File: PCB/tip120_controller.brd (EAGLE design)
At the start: 52.4 x 37.5 mm, 14 parts, among them J1 AUDIO_JACK_3.5MM_PTH, Q1 TIP120

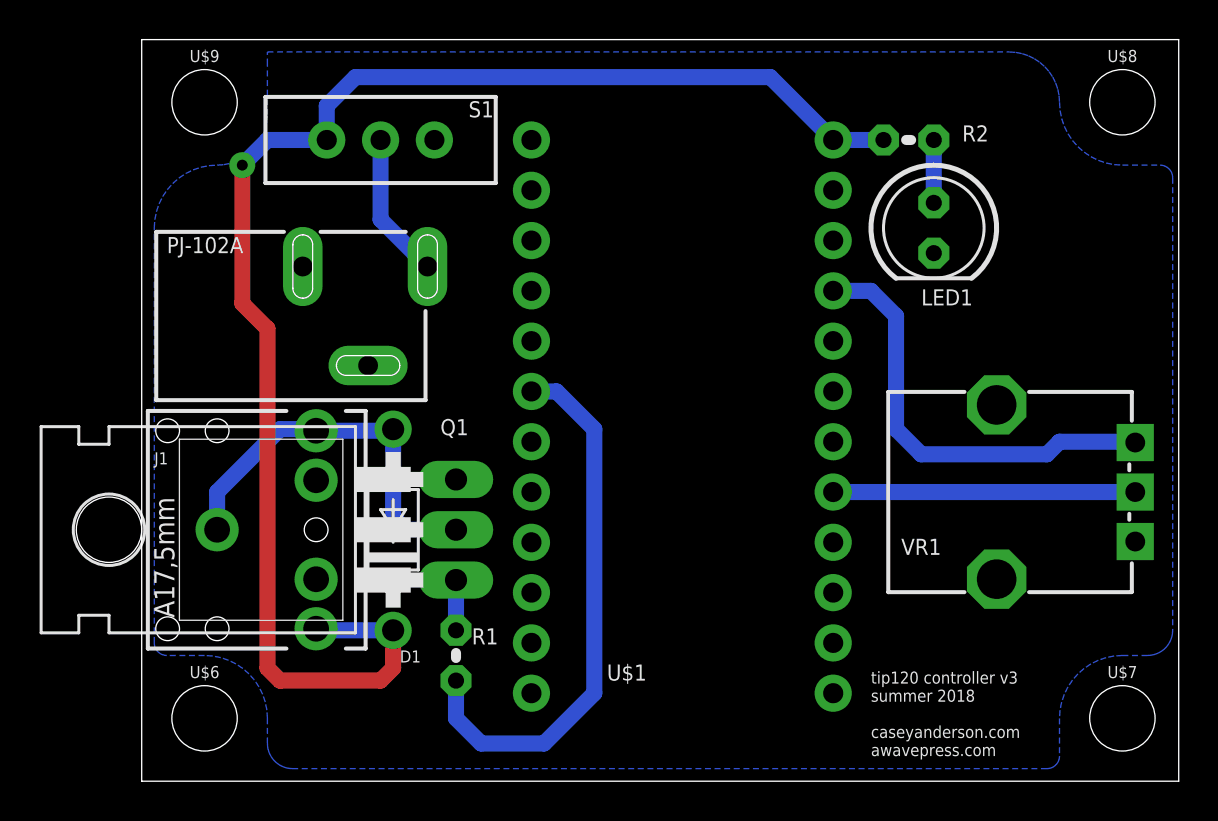
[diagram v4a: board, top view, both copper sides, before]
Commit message: replaced transistor symbol/footprint, futzing with silkscreen
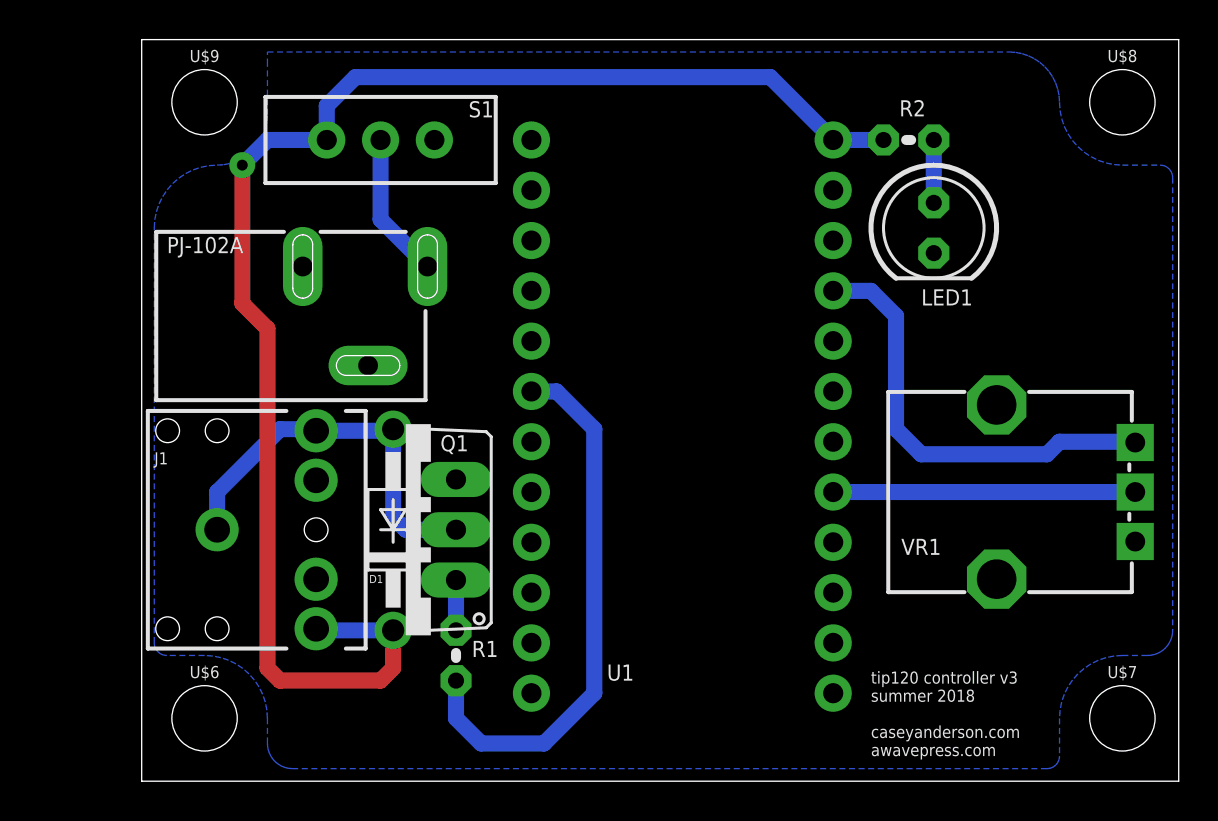
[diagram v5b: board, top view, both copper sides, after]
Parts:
- Q1: device transistor-power:TO220AH -> transistor-power:TO220AV
- moved Q1 3.81 mm to (12.7, 59.1)
- renumbered U$1 to U1
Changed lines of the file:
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@@
 </autorouter>
 <elements>
-<element name="U$1" library="SparkFun-Boards" package="ARDUINO_MINI" value="ARDUINO_MINI" x="26.67" y="66.04" smashed="yes">
+<element name="U1" library="SparkFun-Boards" package="ARDUINO_MINI" value="ARDUINO_MINI" x="26.67" y="66.04" smashed="yes">
 <attribute name="NAME" x="22.86" y="51.435" size="0.8128" layer="25" font="vector" ratio="15"/>
 <attribute name="VALUE" x="22.86" y="50.165" size="0.8128" layer="27" font="vector" ratio="15"/>
@@
 <attribute name="PROD_ID" value="SWCH-08261" x="11.43" y="78.74" size="1.778" layer="27" rot="R270" display="off"/>
 <attribute name="SF_SKU" value="COM-00102" x="11.43" y="78.74" size="1.778" layer="27" rot="R270" display="off"/>
-<attribute name="VALUE" x="15.24" y="77.597" size="0.8128" layer="27" font="vector" ratio="15" align="top-center"/>
 </element>
 <element name="R2" library="resistor" library_urn="urn:adsk.eagle:library:348" package="0204V" package3d_urn="urn:adsk.eagle:package:25948/1" value="220" x="38.1" y="78.74" smashed="yes" rot="R180">
-<attribute name="NAME" x="42.1386" y="79.4766" size="0.8128" layer="25" font="vector" ratio="15" rot="R180"/>
-<attribute name="VALUE" x="42.7736" y="78.5114" size="0.8128" layer="27" font="vector" ratio="15" rot="R180"/>
+<attribute name="NAME" x="38.9636" y="80.7466" size="0.8128" layer="25" font="vector" ratio="15" rot="R180"/>
 </element>
 <element name="LED1" library="led" library_urn="urn:adsk.eagle:library:259" package="LED5MM" package3d_urn="urn:adsk.eagle:package:15799/2" value="" x="39.37" y="74.295" smashed="yes" rot="R270">
 <attribute name="NAME" x="38.735" y="70.3834" size="0.8128" layer="25" font="vector" ratio="15"/>
 </element>
-<element name="Q1" library="transistor-power" library_urn="urn:adsk.eagle:library:400" package="TO220AH" package3d_urn="urn:adsk.eagle:package:29488/1" value="TIP120" x="8.89" y="59.055" smashed="yes" rot="R90">
-<attribute name="NAME" x="15.875" y="64.643" size="0.8128" layer="25" font="vector" ratio="15" rot="R180"/>
-<attribute name="VALUE" x="17.272" y="63.5" size="0.8128" layer="27" font="vector" ratio="15" rot="R180"/>
-</element>
 <element name="R1" library="resistor" library_urn="urn:adsk.eagle:library:348" package="0204V" package3d_urn="urn:adsk.eagle:package:25948/1" value="2.2k" x="15.24" y="52.705" smashed="yes" rot="R270">
-<attribute name="NAME" x="17.3736" y="54.0766" size="0.8128" layer="25" font="vector" ratio="15" rot="R180"/>
-<attribute name="VALUE" x="17.3736" y="53.1114" size="0.8128" layer="27" font="vector" ratio="15" rot="R180"/>
+<attribute name="NAME" x="17.3736" y="53.4416" size="0.8128" layer="25" font="vector" ratio="15" rot="R180"/>
 </element>
 <element name="J1" library="SparkFun-Connectors" package="AUDIO-JACK" value="AUDIO_JACK_3.5MM_PTH" x="3.175" y="59.055" smashed="yes">
@@
 </element>
 <element name="D1" library="diode" library_urn="urn:adsk.eagle:library:210" package="DO41-10" package3d_urn="urn:adsk.eagle:package:43336/1" value="1N4004" x="12.065" y="59.055" smashed="yes" rot="R90">
-<attribute name="NAME" x="13.462" y="52.959" size="0.6096" layer="25" font="vector" ratio="15" rot="R180"/>
+<attribute name="NAME" x="11.557" y="56.769" size="0.4064" layer="25" font="vector" ratio="15" rot="R180"/>
 </element>
 <element name="U$6" library="SparkFun-Hardware" package="STAND-OFF" value="" x="2.54" y="49.53"/>
@@
 <element name="U$8" library="SparkFun-Hardware" package="STAND-OFF" value="" x="48.895" y="80.645"/>
 <element name="U$9" library="SparkFun-Hardware" package="STAND-OFF" value="" x="2.54" y="80.645"/>
+<element name="Q1" library="transistor-power" library_urn="urn:adsk.eagle:library:400" package="TO220AV" package3d_urn="urn:adsk.eagle:package:29487/2" value="TIP120" x="12.7" y="59.055" smashed="yes" rot="R90">
+<attribute name="NAME" x="15.875" y="63.8302" size="0.8128" layer="25" font="vector" ratio="15" rot="R180"/>
+</element>
 </elements>
 <signals>
 <signal name="AGND">
-<contactref element="U$1" pad="23"/>
+<contactref element="U1" pad="23"/>
 <contactref element="LED1" pad="K"/>
 <contactref element="PJ-102A" pad="3"/>
 <contactref element="PJ-102A" pad="2"/>
-<contactref element="Q1" pad="E"/>
-<contactref element="U$1" pad="4"/>
+<contactref element="U1" pad="4"/>
 <contactref element="VR1" pad="P$1"/>
 <polygon width="0.254" layer="16" isolate="0.8128">
@@
 <vertex x="5.715" y="82.55"/>
 </polygon>
+<contactref element="Q1" pad="E"/>
 </signal>
 <signal name="N$3">
@@
 <wire x1="11.43" y1="74.72" x2="11.43" y2="78.74" width="0.8128" layer="16"/>
 </signal>
-<signal name="N$2">
-<contactref element="Q1" pad="B"/>
-<contactref element="R1" pad="1"/>
-<wire x1="15.24" y1="53.975" x2="15.24" y2="56.515" width="0.8128" layer="16"/>
-</signal>
 <signal name="N$8">
 <contactref element="S1" pad="3"/>
 <contactref element="R2" pad="2"/>
-<contactref element="U$1" pad="24"/>
+<contactref element="U1" pad="24"/>
 <wire x1="34.29" y1="78.74" x2="36.83" y2="78.74" width="0.8128" layer="16"/>
 <contactref element="J1" pad="TIP"/>
@@
 <signal name="N$1">
 <contactref element="R1" pad="2"/>
-<contactref element="U$1" pad="6"/>
+<contactref element="U1" pad="6"/>
 <wire x1="22.225" y1="50.8" x2="22.225" y2="64.135" width="0.8128" layer="16"/>
 <wire x1="22.225" y1="64.135" x2="20.32" y2="66.04" width="0.8128" layer="16"/>
@@
 <contactref element="J1" pad="RING"/>
 <contactref element="J1" pad="SLEEVE"/>
-<contactref element="Q1" pad="C"/>
 <contactref element="D1" pad="A"/>
 <wire x1="3.175" y1="59.055" x2="3.175" y2="60.96" width="0.8128" layer="16"/>
@@
 <wire x1="8.175" y1="64.055" x2="11.985" y2="64.055" width="0.8128" layer="16"/>
 <wire x1="11.985" y1="64.055" x2="12.065" y2="64.135" width="0.8128" layer="16"/>
-<wire x1="15.24" y1="59.055" x2="12.7" y2="59.055" width="0.8128" layer="16"/>
-<wire x1="12.7" y1="59.055" x2="12.065" y2="59.69" width="0.8128" layer="16"/>
+<wire x1="12.065" y1="59.69" x2="12.7" y2="59.055" width="0.8128" layer="16"/>
 <wire x1="12.065" y1="59.69" x2="12.065" y2="64.135" width="0.8128" layer="16"/>
+<contactref element="Q1" pad="C"/>
+<wire x1="12.7" y1="59.055" x2="15.24" y2="59.055" width="0.8128" layer="16"/>
 </signal>
 <signal name="N$5">
-<contactref element="U$1" pad="21"/>
+<contactref element="U1" pad="21"/>
 <contactref element="VR1" pad="P$3"/>
 <wire x1="34.29" y1="71.12" x2="36.195" y2="71.12" width="0.8128" layer="16"/>
@@
 <signal name="N$6">
 <contactref element="VR1" pad="P$2"/>
-<contactref element="U$1" pad="17"/>
+<contactref element="U1" pad="17"/>
 <wire x1="49.545" y1="60.96" x2="34.29" y2="60.96" width="0.8128" layer="16"/>
 </signal>
+<signal name="N$2">
+<contactref element="Q1" pad="B"/>
+<contactref element="R1" pad="1"/>
+<wire x1="15.24" y1="53.975" x2="15.24" y2="56.515" width="0.8128" layer="16"/>
+</signal>
 </signals>

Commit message: sanity check
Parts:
- LED1: value (none) -> RED
- S1: value 6-12V -> EG1218
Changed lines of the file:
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@@
 <attribute name="VALUE" x="0.635" y="71.755" size="0.8128" layer="27" font="vector" ratio="15"/>
-</element>
-<element name="S1" library="SparkFun-Switches" package="SWITCH_SPDT_PTH_11.6X4.0MM_KIT" value="6-12V" x="11.43" y="78.74" smashed="yes" rot="R270">
-<attribute name="NAME" x="16.51" y="79.883" size="0.8128" layer="25" font="vector" ratio="15" align="bottom-center"/>
-<attribute name="PROD_ID" value="SWCH-08261" x="11.43" y="78.74" size="1.778" layer="27" rot="R270" display="off"/>
-<attribute name="SF_SKU" value="COM-00102" x="11.43" y="78.74" size="1.778" layer="27" rot="R270" display="off"/>
 </element>
 <element name="R2" library="resistor" library_urn="urn:adsk.eagle:library:348" package="0204V" package3d_urn="urn:adsk.eagle:package:25948/1" value="220" x="38.1" y="78.74" smashed="yes" rot="R180">
 <attribute name="NAME" x="38.9636" y="80.7466" size="0.8128" layer="25" font="vector" ratio="15" rot="R180"/>
 </element>
-<element name="LED1" library="led" library_urn="urn:adsk.eagle:library:259" package="LED5MM" package3d_urn="urn:adsk.eagle:package:15799/2" value="" x="39.37" y="74.295" smashed="yes" rot="R270">
+<element name="LED1" library="led" library_urn="urn:adsk.eagle:library:259" package="LED5MM" package3d_urn="urn:adsk.eagle:package:15799/2" value="RED" x="39.37" y="74.295" smashed="yes" rot="R270">
 <attribute name="NAME" x="38.735" y="70.3834" size="0.8128" layer="25" font="vector" ratio="15"/>
 </element>
@@
 <element name="Q1" library="transistor-power" library_urn="urn:adsk.eagle:library:400" package="TO220AV" package3d_urn="urn:adsk.eagle:package:29487/2" value="TIP120" x="12.7" y="59.055" smashed="yes" rot="R90">
 <attribute name="NAME" x="15.875" y="63.8302" size="0.8128" layer="25" font="vector" ratio="15" rot="R180"/>
+</element>
+<element name="S1" library="SparkFun-Switches" package="SWITCH_SPDT_PTH_11.6X4.0MM_KIT" value="EG1218" x="11.43" y="78.74" smashed="yes" rot="R270">
+<attribute name="NAME" x="16.51" y="77.978" size="0.6096" layer="25" font="vector" ratio="20" align="bottom-center"/>
+<attribute name="PROD_ID" value="SWCH-08261" x="11.43" y="78.74" size="1.778" layer="27" rot="R270" display="off"/>
+<attribute name="SF_SKU" value="COM-00102" x="11.43" y="78.74" size="1.778" layer="27" rot="R270" display="off"/>
+<attribute name="VALUE" x="15.24" y="77.597" size="0.6096" layer="27" font="vector" ratio="20" align="top-center"/>
 </element>
 </elements>
@@
 <signal name="N$7">
 <contactref element="PJ-102A" pad="1"/>
+<wire x1="13.8" y1="72.35" x2="11.43" y2="74.72" width="0.8128" layer="16"/>
 <contactref element="S1" pad="2"/>
-<wire x1="13.8" y1="72.35" x2="11.43" y2="74.72" width="0.8128" layer="16"/>
 <wire x1="11.43" y1="74.72" x2="11.43" y2="78.74" width="0.8128" layer="16"/>
 </signal>
 <signal name="N$8">
-<contactref element="S1" pad="3"/>
 <contactref element="R2" pad="2"/>
 <contactref element="U1" pad="24"/>
@@
 <wire x1="8.175" y1="54.055" x2="8.255" y2="53.975" width="0.8128" layer="16"/>
 <wire x1="8.255" y1="53.975" x2="12.065" y2="53.975" width="0.8128" layer="16"/>
-<wire x1="8.7122" y1="78.74" x2="8.7122" y2="80.4672" width="0.8128" layer="16"/>
 <wire x1="8.7122" y1="80.4672" x2="10.16" y2="81.915" width="0.8128" layer="16"/>
 <wire x1="10.16" y1="81.915" x2="31.115" y2="81.915" width="0.8128" layer="16"/>
@@
 <wire x1="4.445" y1="70.485" x2="4.445" y2="77.47" width="0.8128" layer="1"/>
 <wire x1="4.445" y1="77.47" x2="5.715" y2="78.74" width="0.8128" layer="16"/>
+<contactref element="S1" pad="3"/>
 <wire x1="5.715" y1="78.74" x2="8.7122" y2="78.74" width="0.8128" layer="16"/>
+<wire x1="8.7122" y1="78.74" x2="8.7122" y2="80.4672" width="0.8128" layer="16"/>
 </signal>
 <signal name="N$1">
